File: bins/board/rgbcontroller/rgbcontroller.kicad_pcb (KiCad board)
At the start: 2 copper layers, 71.8 x 43.8 mm, 24 parts, among them Q1 BD139, Q2 BD139, Q3 BD139, U1 ESP-12E

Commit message: PCB adjustments
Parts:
- added G***: LOGO, WiFi_Strips_Logo:wifilogo, B.Cu at (149.2, 59.7)
- added REF**: logo, WiFi_Strips_Logo:logo, F.Cu at (0.00, 0.00)
- C1, C2, MODE, Q1, Q2, Q3, R1, R2, R2B1, R3, R4, R5, R6, R7, R8, R9, RV1: moved to B.Cu
- Prog: renamed from Programmer; moved to B.Cu
- RST: renamed from RESET; value SW_Push -> RST; moved to B.Cu
- Strip-Plug: renamed from Strip-Connector1; moved to B.Cu
- moved RST 6.54 mm to (125.1, 48.9), turned to 0 degrees
- moved MODE 6.36 mm to (167.1, 64.8), turned to 90 degrees
- moved RV1 5.04 mm to (120.7, 52.0)
- moved R9 0.25 mm to (159.4, 63.8)
- turned Prog to 0 degrees
- turned Strip-Plug to 180 degrees
- renumbered Regulador12a3.3 to 12-3.3V, SWSup1 to MasterSW
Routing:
- net GND: track 172.9 -> 177.1 mm

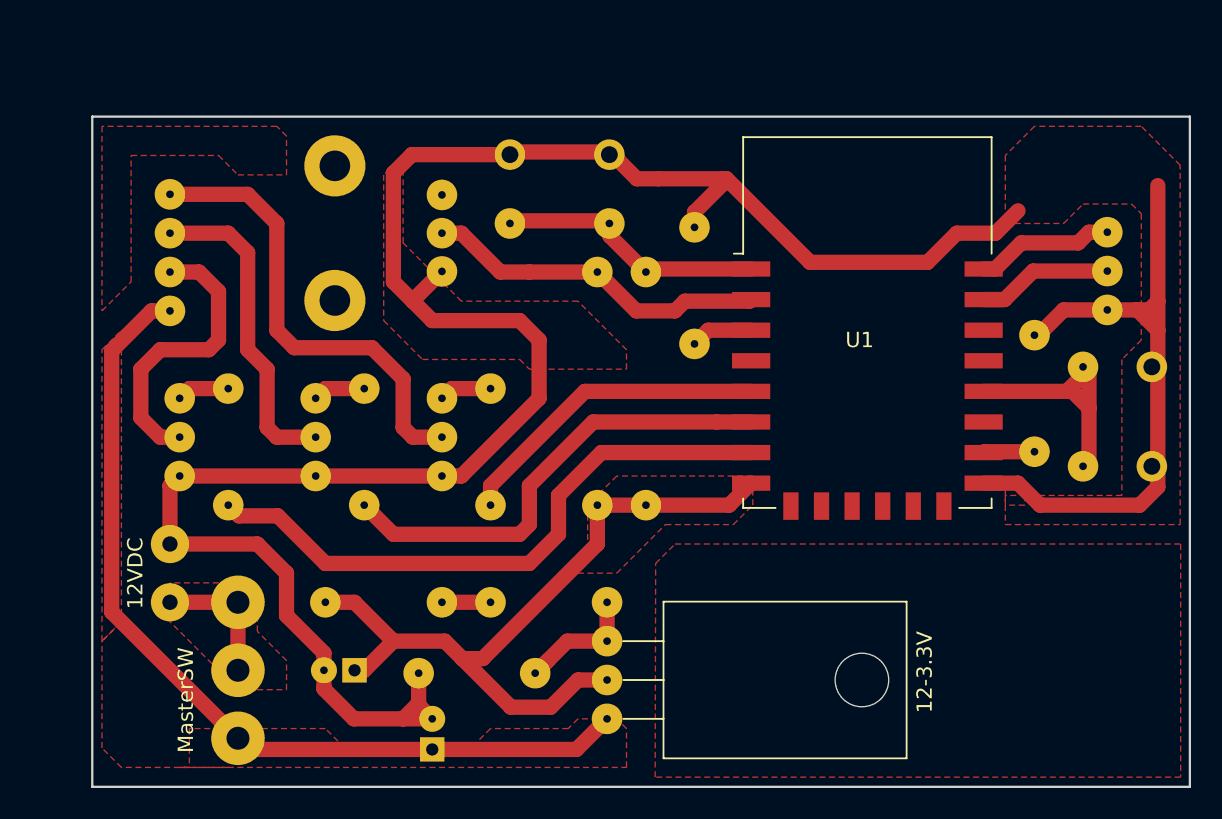
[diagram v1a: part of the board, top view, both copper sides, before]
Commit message: Minor screws adjustments
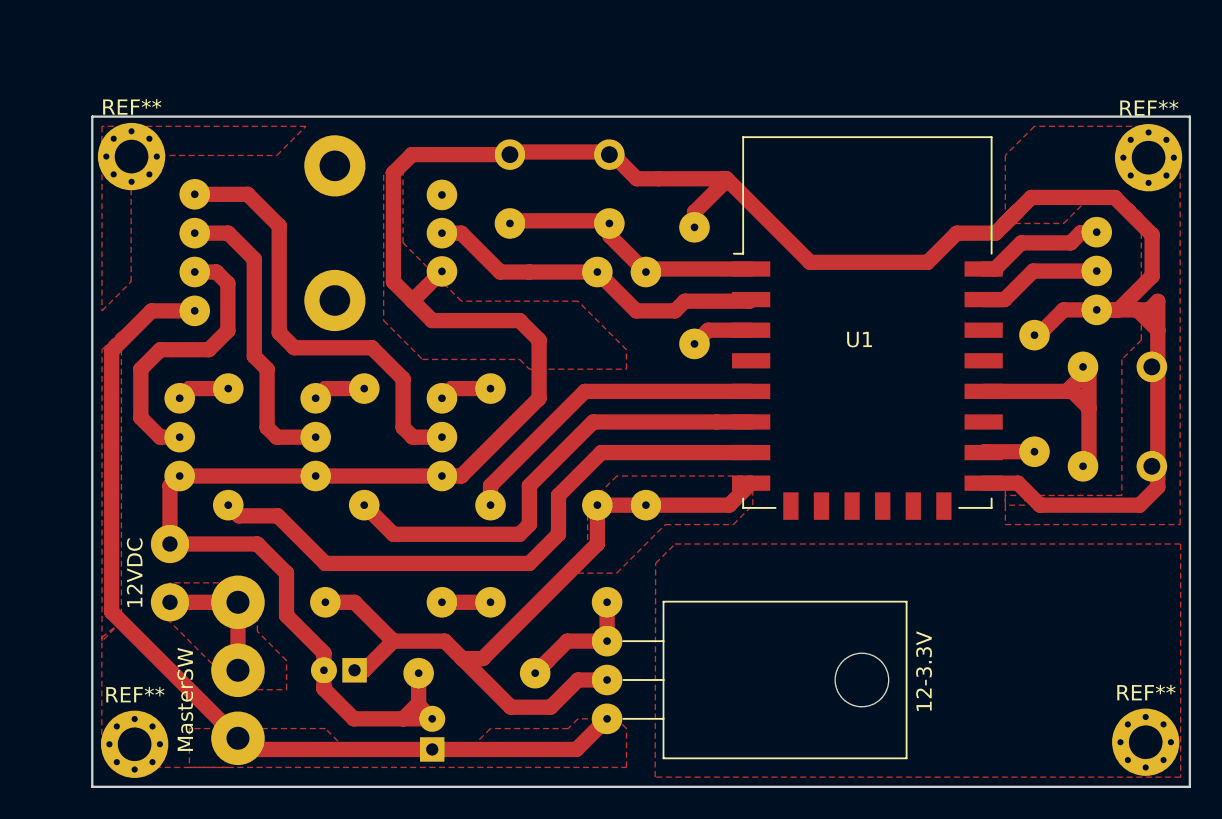
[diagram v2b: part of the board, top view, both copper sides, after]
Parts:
- added REF**: MountingHole_2.2mm_M2_Pad_Via, Mounting_Holes:MountingHole_2.2mm_M2_Pad_Via, F.Cu at (100.4, 44.5)
- added REF**: MountingHole_2.2mm_M2_Pad_Via, Mounting_Holes:MountingHole_2.2mm_M2_Pad_Via, F.Cu at (100.6, 82.9)
- added REF**: MountingHole_2.2mm_M2_Pad_Via, Mounting_Holes:MountingHole_2.2mm_M2_Pad_Via, F.Cu at (166.7, 82.8)
- added REF**: MountingHole_2.2mm_M2_Pad_Via, Mounting_Holes:MountingHole_2.2mm_M2_Pad_Via, F.Cu at (166.8, 44.6)
- moved Strip-Plug 1.62 mm to (104.5, 47.0)
- moved Prog 0.69 mm to (163.5, 54.5)
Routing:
- net GND: track 177.1 -> 188.2 mm
- net +12-strip: track 58.9 -> 60.5 mm
- net R-strip: track 21.0 -> 19.4 mm
- net B-strip: track 30.3 -> 28.7 mm
- net Net-(Programmer-Connector1-Pad3): track 9.08 -> 8.39 mm
- net Net-(Programmer-Connector1-Pad2): track 8.86 -> 8.16 mm
